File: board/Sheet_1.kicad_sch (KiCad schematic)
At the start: 24 parts, among them SW1 K2-1830UQ-A4DW-06, SW2 K2-1830UQ-A4DW-06, U1 ESP32-C3FH4, U2 XC6206P332MR, X1 40MHz

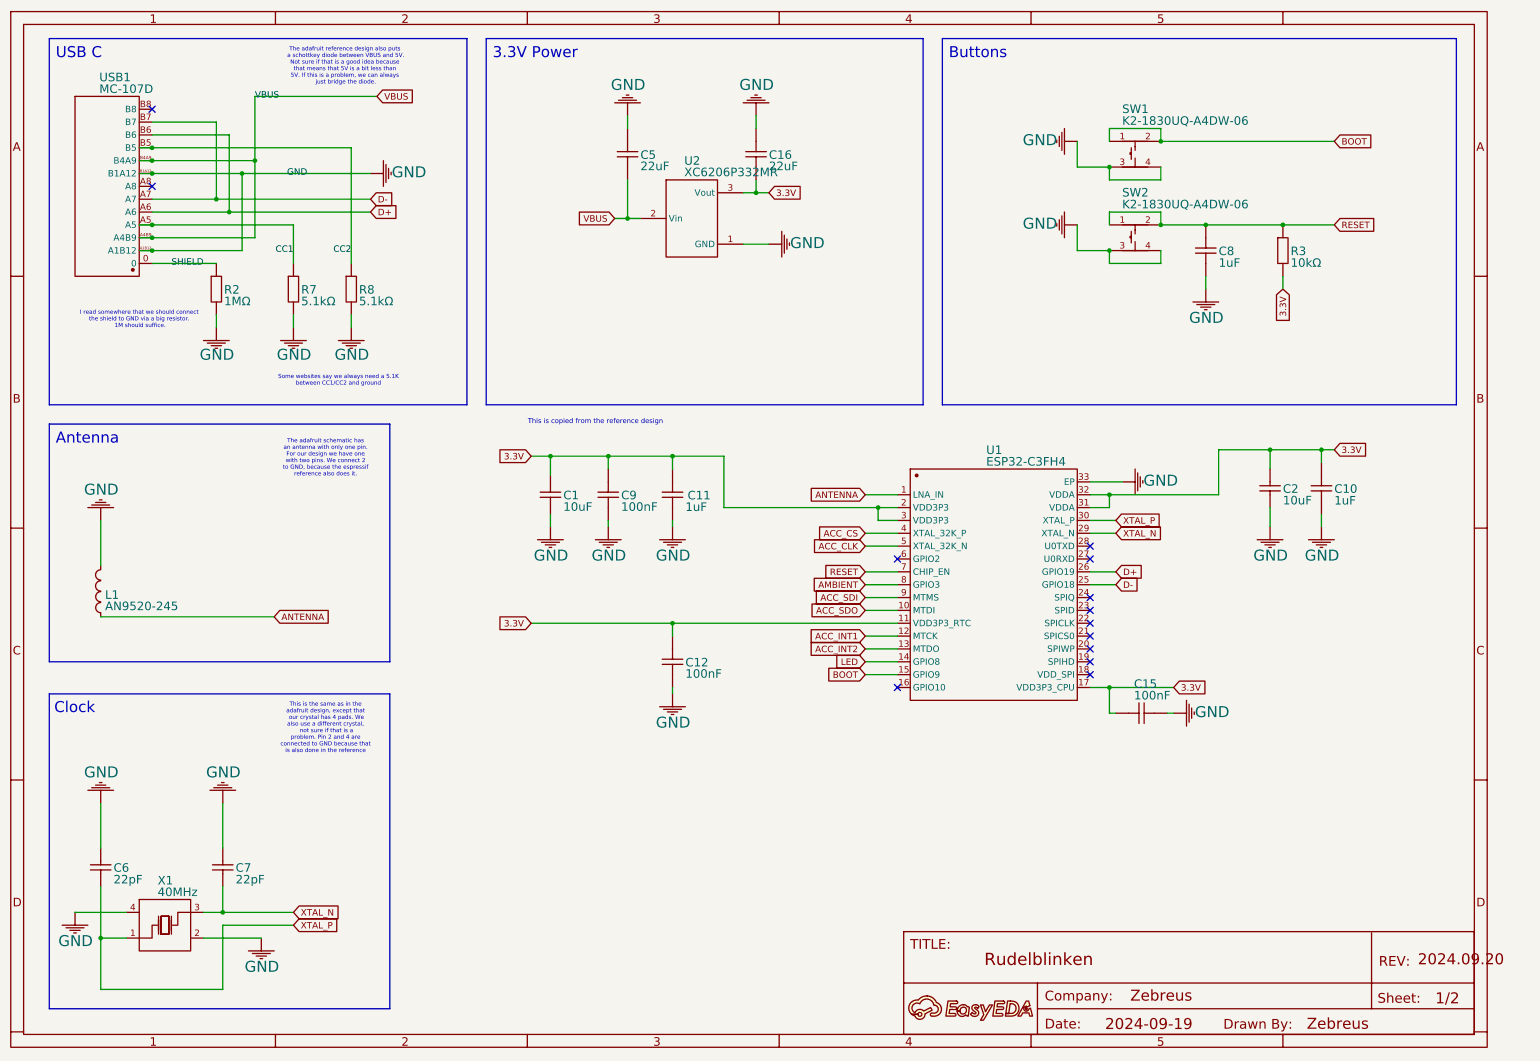
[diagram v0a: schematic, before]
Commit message: Organize schematics for kicad
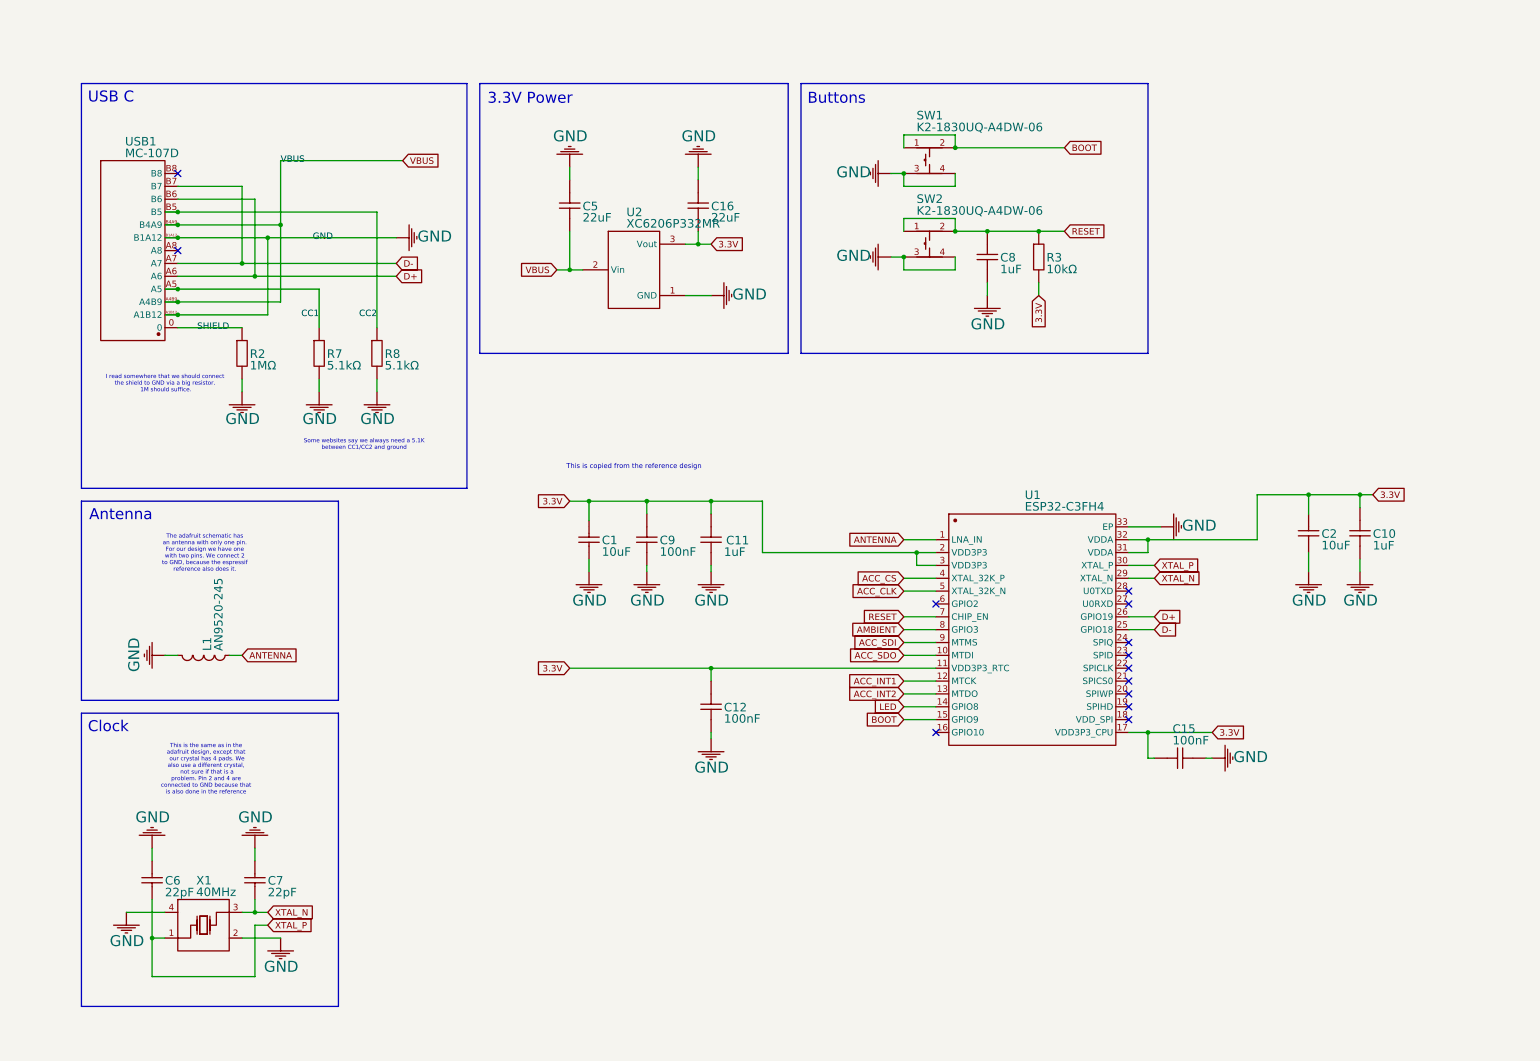
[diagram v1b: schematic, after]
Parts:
- removed A: A, symbol Unknown_0_-806
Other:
- note removed: "The adafruit reference design also puts a schottkey diode between VBUS and 5V. Not sure if that is a good idea because that means that 5V is a bit less than 5V. If this is a problem, we can always just bridge the diode."
- company: (none) -> Zebreus
- title: (none) -> Rudelblinken
- moved on the sheet: C1, C10, C11, C12, C15, C16, C2, C5, C6, C7, C8, C9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
